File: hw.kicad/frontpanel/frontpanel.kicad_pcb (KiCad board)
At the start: 2 copper layers, 133.5 x 32 mm, 14 parts, among them U1 LTP-7357AG, U10 LTP-7357AG, U11 TLC5928, U12 TLC5928, U13 TLC5928, U14 TLC5928, U2 LTP-7357AG, U3 LTP-7357AG, U4 LTP-7357AG, U5 LTP-7357AG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

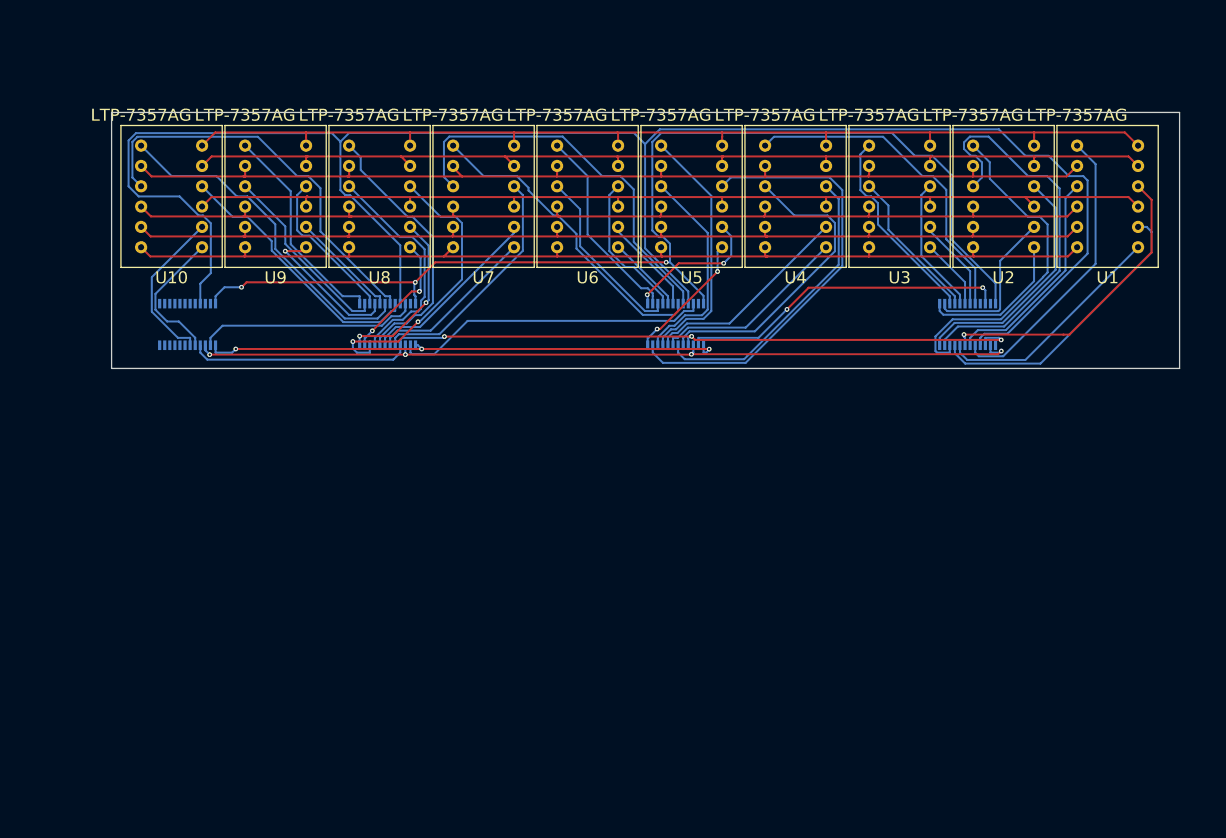
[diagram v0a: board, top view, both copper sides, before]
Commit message: adding frontpanel hw
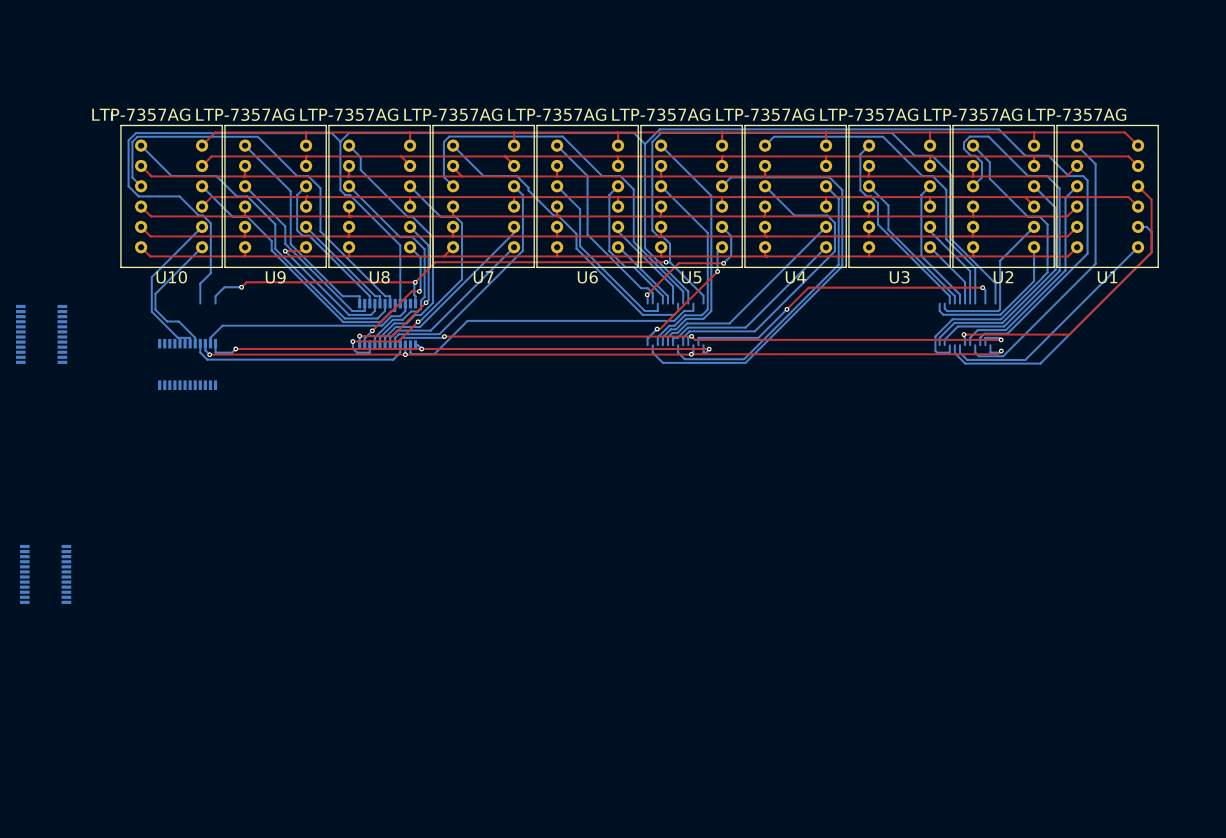
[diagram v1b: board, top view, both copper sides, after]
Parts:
- moved U14 115.8 mm to (71.2, 90.2), turned to 180 degrees
- moved U13 84.7 mm to (71.8, 120.2), turned to 180 degrees
- moved U11 5.00 mm to (89.5, 94.0)
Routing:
- net (no net): track 0.00 -> 758.7 mm, vias 0 -> 15
- net Net-(U11-Pad21): track 227.4 -> 0.00 mm
- net VCC: track 143.9 -> 0.00 mm, vias 3 -> 0
- net Net-(U11-Pad4): track 108.2 -> 0.00 mm, vias 3 -> 0
- net Net-(U11-Pad3): track 105.3 -> 0.00 mm, vias 4 -> 0
- net GND: track 65.6 -> 0.00 mm, vias 3 -> 0
- net Net-(U13-Pad2): track 41.2 -> 0.00 mm, vias 2 -> 0
- net Net-(U12-Pad2): track 39.5 -> 0.00 mm
- net Net-(U11-Pad2): track 27.6 -> 0.00 mm
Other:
- board outline removed

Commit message: update files
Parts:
- added P1: CONN_10, Pin_Headers:Pin_Header_Straight_1x10, F.Cu at (139.7, 130.8)
- added P2: CONN_10, Pin_Headers:Pin_Header_Straight_1x10, F.Cu at (170.2, 68.6)
- added P3: CONN_10, Pin_Headers:Pin_Header_Straight_1x10, F.Cu at (118.0, 68.8)
- added P4: CONN_10, Pin_Headers:Pin_Header_Straight_1x10, F.Cu at (143.2, 68.8)
- added P5: CONN_10, Pin_Headers:Pin_Header_Straight_1x10, F.Cu at (91.4, 68.6)
- added P6: CONN_10, Pin_Headers:Pin_Header_Straight_1x10, F.Cu at (209.6, 52.1)
- added P7: CONN_8, Pin_Headers:Pin_Header_Straight_1x08, F.Cu at (97.8, 111.8)
- added P8: CONN_8, Pin_Headers:Pin_Header_Straight_1x08, F.Cu at (82.5, 68.6)
- added R1: R, Resistors_SMD:R_0805, F.Cu at (100.2, 135.8)
- added R2: R, Resistors_SMD:R_0805, F.Cu at (185.8, 120.5)
- added R3: R, Resistors_SMD:R_0805, F.Cu at (167.8, 118.2)
- added R4: R, Resistors_SMD:R_0805, F.Cu at (161.8, 149.0)
- added U15: MIC2981, Housings_SOIC:SOIC-18_7.5x11.6mm_Pitch1.27mm, F.Cu at (83.0, 125.8)
- added U16: DSPIC33FJ64GP802, Housings_DFN_QFN:QFN-28-1EP_6x6mm_Pitch0.65mm, F.Cu at (184.2, 138.8)
- U11, U12, U13, U14: moved to F.Cu
- moved U10 120.9 mm to (208.2, 78.8)
- moved U1 113.4 mm to (91.2, 78.8)
- moved U9 94.9 mm to (195.2, 78.8)
- moved U11 90.2 mm to (168.5, 137.5)
- moved U2 87.4 mm to (104.2, 78.8)
- moved U8 69.0 mm to (182.2, 78.8)
- moved U12 65.6 mm to (143.2, 148.0), turned to 270 degrees
- moved U3 61.5 mm to (117.2, 78.8)
- moved U13 58.0 mm to (126.2, 140.0), turned to 90 degrees
- moved U14 54.2 mm to (111.5, 126.5), turned to 90 degrees
- moved U7 43.1 mm to (169.2, 78.8)
- moved U4 35.7 mm to (130.2, 78.8)
- moved U6 17.7 mm to (156.2, 78.8)
- moved U5 10.9 mm to (143.2, 78.8)
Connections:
- U1 pad 1: /COL1 -> (no net)
- U1 pad 10: /COL3 -> (no net)
- U1 pad 3: /COL2 -> (no net)
- U1 pad 7: /COL4 -> (no net)
- U1 pad 8: /COL5 -> (no net)
- U10 pad 1: /COL46 -> (no net)
- U10 pad 10: /COL48 -> (no net)
- U10 pad 3: /COL47 -> (no net)
- U10 pad 7: /COL49 -> (no net)
- U10 pad 8: /COL50 -> (no net)
- U11 pad 23: (no net) -> Net-(R2-Pad1)
- U11 pad 5: /COL49 -> (no net)
- U11 pad 6: /COL50 -> (no net)
- U12 pad 10: /COL38 -> (no net)
- U12 pad 11: /COL39 -> (no net)
- U12 pad 12: /COL40 -> (no net)
- U12 pad 13: /COL41 -> (no net)
- U12 pad 14: /COL42 -> (no net)
- U12 pad 15: /COL43 -> (no net)
- U12 pad 16: /COL44 -> (no net)
- U12 pad 17: /COL45 -> (no net)
- U12 pad 18: /COL46 -> (no net)
- U12 pad 19: /COL47 -> (no net)
- U12 pad 20: /COL48 -> (no net)
- U12 pad 23: (no net) -> Net-(R3-Pad1)
- U12 pad 5: /COL33 -> (no net)
- U12 pad 6: /COL34 -> (no net)
- U12 pad 7: /COL35 -> (no net)
- U12 pad 8: /COL36 -> (no net)
- U12 pad 9: /COL37 -> (no net)
- U13 pad 10: /COL22 -> (no net)
- U13 pad 11: /COL23 -> (no net)
- U13 pad 12: /COL24 -> (no net)
- U13 pad 13: /COL25 -> (no net)
- U13 pad 14: /COL26 -> (no net)
- U13 pad 15: /COL27 -> (no net)
- U13 pad 16: /COL28 -> (no net)
- U13 pad 17: /COL29 -> (no net)
- U13 pad 18: /COL30 -> (no net)
- U13 pad 19: /COL31 -> (no net)
- U13 pad 20: /COL32 -> (no net)
- U13 pad 23: (no net) -> Net-(R4-Pad1)
- U13 pad 5: /COL17 -> (no net)
- U13 pad 6: /COL18 -> (no net)
- U13 pad 7: /COL19 -> (no net)
- U13 pad 8: /COL20 -> (no net)
- U13 pad 9: /COL21 -> (no net)
- U14 pad 1: (no net) -> GND
- U14 pad 10: /COL6 -> (no net)
- U14 pad 11: /COL7 -> (no net)
- U14 pad 12: /COL8 -> (no net)
- U14 pad 13: /COL9 -> (no net)
- U14 pad 14: /COL10 -> (no net)
- U14 pad 15: /COL11 -> (no net)
- U14 pad 16: /COL12 -> (no net)
- U14 pad 17: /COL13 -> (no net)
- U14 pad 18: /COL14 -> (no net)
- U14 pad 19: /COL15 -> (no net)
- U14 pad 20: /COL16 -> (no net)
- U14 pad 23: (no net) -> Net-(R1-Pad1)
- U14 pad 5: /COL1 -> (no net)
- U14 pad 6: /COL2 -> (no net)
- U14 pad 7: /COL3 -> (no net)
- U14 pad 8: /COL4 -> (no net)
- U14 pad 9: /COL5 -> (no net)
- U2 pad 1: /COL6 -> (no net)
- U2 pad 10: /COL8 -> (no net)
- U2 pad 3: /COL7 -> (no net)
- U2 pad 7: /COL9 -> (no net)
- U2 pad 8: /COL10 -> (no net)
- U3 pad 1: /COL11 -> (no net)
- U3 pad 10: /COL13 -> (no net)
- U3 pad 3: /COL12 -> (no net)
- U3 pad 7: /COL14 -> (no net)
- U3 pad 8: /COL15 -> (no net)
- U4 pad 1: /COL16 -> (no net)
- U4 pad 10: /COL18 -> (no net)
- U4 pad 3: /COL17 -> (no net)
- U4 pad 7: /COL19 -> (no net)
- U4 pad 8: /COL20 -> (no net)
- U5 pad 1: /COL21 -> (no net)
- U5 pad 10: /COL23 -> (no net)
- U5 pad 3: /COL22 -> (no net)
- U5 pad 7: /COL24 -> (no net)
- U5 pad 8: /COL25 -> (no net)
- U6 pad 1: /COL26 -> (no net)
- U6 pad 10: /COL28 -> (no net)
- U6 pad 3: /COL27 -> (no net)
- U6 pad 7: /COL29 -> (no net)
- U6 pad 8: /COL30 -> (no net)
- U7 pad 1: /COL31 -> (no net)
- U7 pad 10: /COL33 -> (no net)
- U7 pad 3: /COL32 -> (no net)
- U7 pad 7: /COL34 -> (no net)
- U7 pad 8: /COL35 -> (no net)
- U8 pad 1: /COL36 -> (no net)
- U8 pad 10: /COL38 -> (no net)
- U8 pad 3: /COL37 -> (no net)
- U8 pad 7: /COL39 -> (no net)
- U8 pad 8: /COL40 -> (no net)
- U9 pad 1: /COL41 -> (no net)
- U9 pad 10: /COL43 -> (no net)
- U9 pad 3: /COL42 -> (no net)
- U9 pad 7: /COL44 -> (no net)
- U9 pad 8: /COL45 -> (no net)
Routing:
- net (no net): track 758.7 -> 0.00 mm, vias 15 -> 0
- net /ROW1: track 131.6 -> 0.00 mm
- net /ROW3: track 129.5 -> 0.00 mm
- net /ROW2: track 128.8 -> 0.00 mm
- net /ROW5: track 128.8 -> 0.00 mm
- net /ROW4: track 128.4 -> 0.00 mm
- net /ROW6: track 128.3 -> 0.00 mm
- net /ROW7: track 128.1 -> 0.00 mm
- net /COL23: track 55.8 -> 0.00 mm
- net /COL7: track 51.1 -> 0.00 mm
- net /COL47: track 50.8 -> 0.00 mm
- net /COL32: track 49.6 -> 0.00 mm
- net /COL6: track 42.6 -> 0.00 mm
- net /COL46: track 42.6 -> 0.00 mm
- net /COL16: track 41.6 -> 0.00 mm
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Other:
- board outline added: 137 x 33.8 mm
